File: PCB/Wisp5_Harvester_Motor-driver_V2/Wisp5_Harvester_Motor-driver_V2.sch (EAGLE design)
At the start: 27 parts, among them M1 PINHEAD_PINHD-1X2-1.27MM, M2 PINHEAD_PINHD-1X2-1.27MM, U1 BQ25570

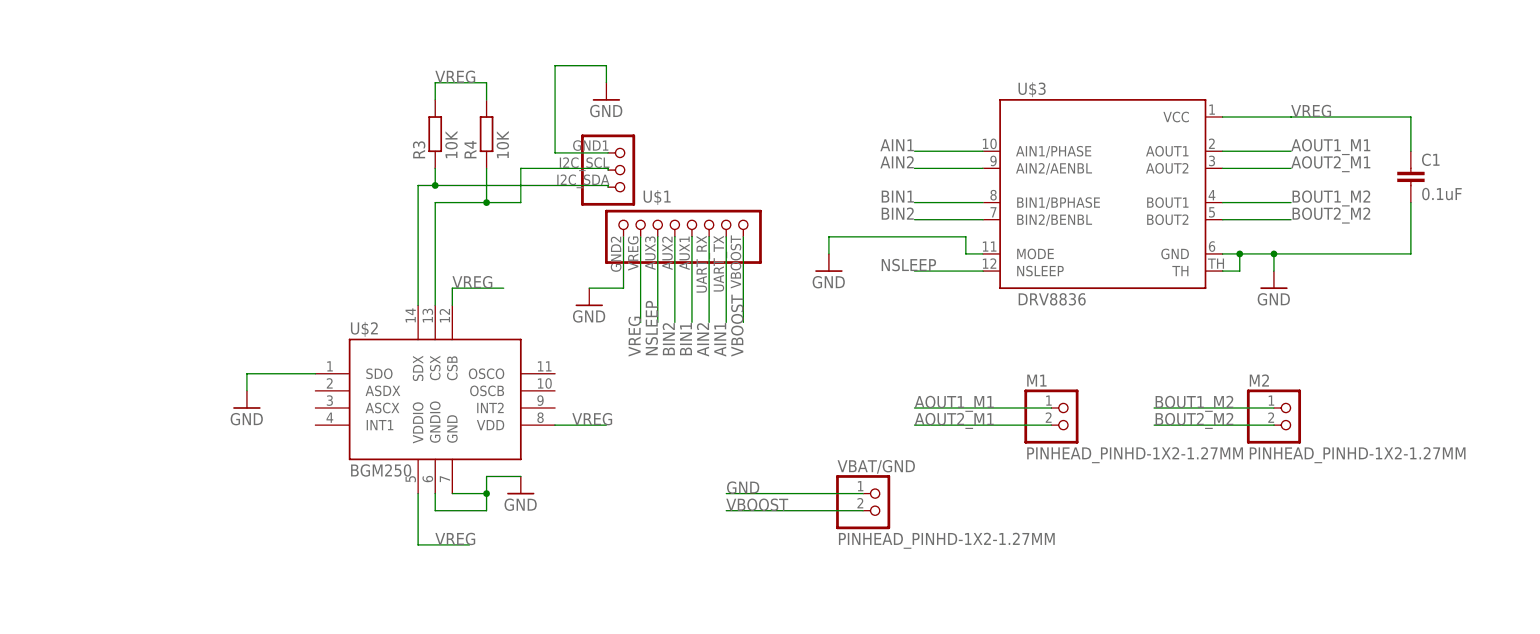
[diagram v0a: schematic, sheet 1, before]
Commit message: Added proximity header and fixed layout
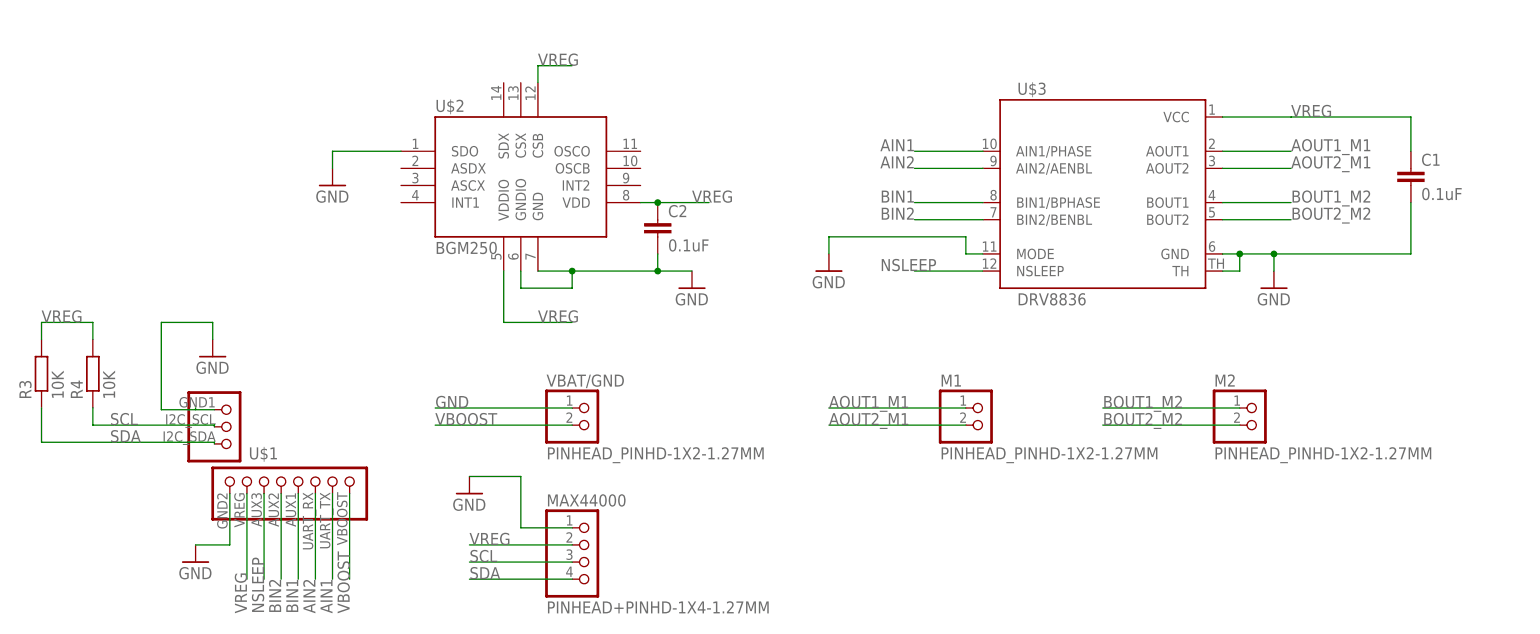
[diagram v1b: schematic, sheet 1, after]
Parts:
- added C2: 0.1uF, rcl:C-EUC0805
- added MAX44000: PINHEAD+PINHD-1X4-1.27MM, Wisp5_Harvester_Motor-driver_V2:PINHEAD+PINHD-1X4-1.27MM
- L1: value (none) -> 22uH
- L2: value (none) -> 10uH
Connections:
- net GND: now also C2.2, MAX44000.1
- net SCL: now also MAX44000.3; no longer U$2.CSX
- net SDA: now also MAX44000.4; no longer U$2.SDX
- net VREG: now also C2.1, MAX44000.2
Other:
- moved on the sheet: M1, M2, R3, R4, U$1, U$2, VBAT/GND

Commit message: Update schematic
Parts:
- U$3: device robot_pcb2:DRV8836 -> Wisp5_Harvester_Motor-driver_V2:DRV8836
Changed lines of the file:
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@@
 </classes>
 <parts>
-<part name="U$3" library="robot_pcb2" deviceset="DRV8836" device=""/>
+<part name="U$3" library="Wisp5_Harvester_Motor-driver_V2" deviceset="DRV8836" device=""/>
 <part name="U1" library="texas" deviceset="BQ25570" device=""/>
 <part name="GND1" library="supply1" deviceset="GND" device=""/>

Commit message: Updated packages
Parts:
- U$3: device Wisp5_Harvester_Motor-driver_V2:DRV8836 -> robot_pcb2:DRV8836
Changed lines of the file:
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@@
 </classes>
 <parts>
-<part name="U$3" library="Wisp5_Harvester_Motor-driver_V2" deviceset="DRV8836" device=""/>
+<part name="U$3" library="robot_pcb2" deviceset="DRV8836" device=""/>
 <part name="U1" library="texas" deviceset="BQ25570" device=""/>
 <part name="GND1" library="supply1" deviceset="GND" device=""/>

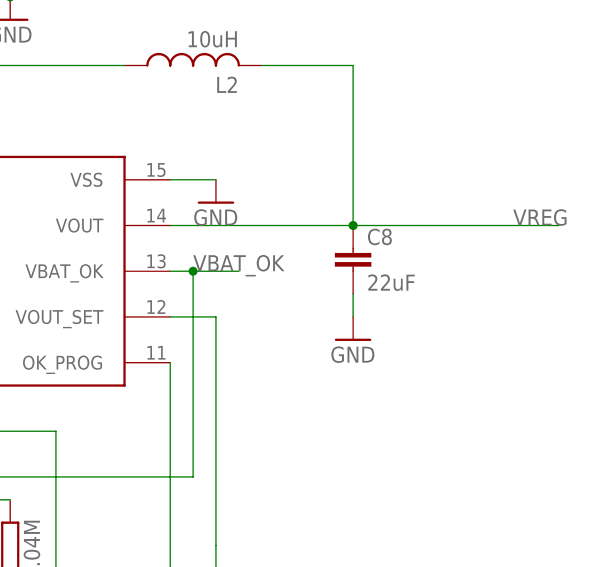
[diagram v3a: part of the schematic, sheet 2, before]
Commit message: Change bulk capacitor from 805 to 1210
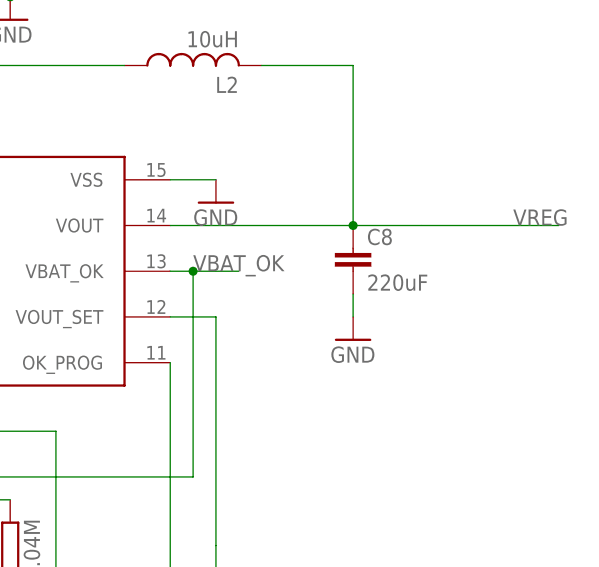
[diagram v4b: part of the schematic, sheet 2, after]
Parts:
- C8: value 22uF -> 220uF; device rcl:C-EUC0805 -> Wisp5_Harvester_Motor-driver_V2:C-EUC1210
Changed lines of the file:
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@@
 <part name="L1" library="robot_pcb2" deviceset="COILCRAFT-LPS4018" device="" value="22uH"/>
 <part name="L2" library="robot_pcb2" deviceset="COILCRAFT-LPS4018" device="" value="10uH"/>
-<part name="C8" library="rcl" deviceset="C-EU" device="C0805" value="22uF"/>
+<part name="C8" library="Wisp5_Harvester_Motor-driver_V2" deviceset="C-EU" device="C1210" value="220uF"/>
 <part name="R6" library="resistor" deviceset="R-EU_" device="R0805" value="6.04M"/>
 <part name="R7" library="resistor" deviceset="R-EU_" device="R0805" value="3.01M"/>

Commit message: Removed some small separate packages
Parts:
- C9: device ipr:BZ054B223ZSBBQ -> Wisp5_Harvester_Motor-driver_V2:BZ054B223ZSBBQ
- U$2: device robot_pcb2:BGM250 -> Wisp5_Harvester_Motor-driver_V2:BGM250
- U1: device texas:BQ25570 -> Wisp5_Harvester_Motor-driver_V2:BQ25570
- VIN/GND: device transceiver:PINHEAD_PINHD-1X2-1.27MM -> Wisp5_Harvester_Motor-driver_V2:PINHEAD_PINHD-1X2-1.27MM
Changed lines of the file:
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@@
 <parts>
 <part name="U$3" library="robot_pcb2" deviceset="DRV8836" device=""/>
-<part name="U1" library="texas" deviceset="BQ25570" device=""/>
+<part name="U1" library="Wisp5_Harvester_Motor-driver_V2" deviceset="BQ25570" device=""/>
 <part name="GND1" library="supply1" deviceset="GND" device=""/>
 <part name="GND5" library="supply1" deviceset="GND" device=""/>
@@
 <part name="GND21" library="supply1" deviceset="GND" device=""/>
 <part name="C4" library="rcl" deviceset="C-EU" device="C0805" value="0.1uF"/>
-<part name="C9" library="ipr" deviceset="BZ054B223ZSBBQ" device=""/>
+<part name="C9" library="Wisp5_Harvester_Motor-driver_V2" deviceset="BZ054B223ZSBBQ" device=""/>
 <part name="R3" library="resistor" deviceset="R-EU_" device="R0805" value="10K"/>
 <part name="R4" library="resistor" deviceset="R-EU_" device="R0805" value="10K"/>
 <part name="GND13" library="supply1" deviceset="GND" device=""/>
 <part name="C1" library="rcl" deviceset="C-EU" device="C0805" value="0.1uF"/>
-<part name="VIN/GND" library="transceiver" deviceset="PINHEAD_PINHD-1X2-1.27MM" device=""/>
+<part name="VIN/GND" library="Wisp5_Harvester_Motor-driver_V2" deviceset="PINHEAD_PINHD-1X2-1.27MM" device=""/>
 <part name="U$1" library="robot_pcb2" deviceset="WISP_HEADER" device=""/>
-<part name="U$2" library="robot_pcb2" deviceset="BGM250" device=""/>
+<part name="U$2" library="Wisp5_Harvester_Motor-driver_V2" deviceset="BGM250" device=""/>
 <part name="GND2" library="supply1" deviceset="GND" device=""/>
 <part name="GND3" library="supply1" deviceset="GND" device=""/>

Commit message: Changed output pins so they work with wisp timer directly and also changed M2 (right)  ground and power order
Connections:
- net AIN1: now also U$1.AUX3; no longer U$1.UART_TX
- net AIN2: now also U$1.AUX1; no longer U$1.UART_RX
- net BIN1: now also U$1.AUX2; no longer U$1.AUX1
- net BIN2: now also U$1.UART_TX; no longer U$1.AUX2
- net BOUT1_M2: now also M2.2; no longer M2.1
- net BOUT2_M2: now also M2.1; no longer M2.2
- net NSLEEP: now also U$1.UART_RX; no longer U$1.AUX3
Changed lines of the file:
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@@
 </segment>
 <segment>
-<pinref part="M2" gate="G$1" pin="1"/>
-<wire x1="180.34" y1="35.56" x2="160.02" y2="35.56" width="0.1524" layer="91"/>
-<label x="160.02" y="35.56" size="1.778" layer="95"/>
+<pinref part="M2" gate="G$1" pin="2"/>
+<wire x1="180.34" y1="33.02" x2="160.02" y2="33.02" width="0.1524" layer="91"/>
+<label x="160.02" y="33.02" size="1.778" layer="95"/>
 </segment>
 </net>
@@
 </segment>
 <segment>
-<pinref part="M2" gate="G$1" pin="2"/>
-<wire x1="180.34" y1="33.02" x2="160.02" y2="33.02" width="0.1524" layer="91"/>
-<label x="160.02" y="33.02" size="1.778" layer="95"/>
+<pinref part="M2" gate="G$1" pin="1"/>
+<wire x1="180.34" y1="35.56" x2="160.02" y2="35.56" width="0.1524" layer="91"/>
+<label x="160.02" y="35.56" size="1.778" layer="95"/>
 </segment>
 </net>
@@
 </segment>
 <segment>
-<pinref part="U$1" gate="G$1" pin="AUX3"/>
-<wire x1="35.56" y1="22.86" x2="35.56" y2="10.16" width="0.1524" layer="91"/>
-<label x="35.56" y="5.08" size="1.778" layer="95" rot="R90"/>
+<pinref part="U$1" gate="G$1" pin="UART_RX"/>
+<wire x1="43.18" y1="22.86" x2="43.18" y2="10.16" width="0.1524" layer="91"/>
+<label x="43.18" y="5.08" size="1.778" layer="95" rot="R90"/>
 </segment>
 </net>
@@
 </segment>
 <segment>
-<pinref part="U$1" gate="G$1" pin="AUX2"/>
-<wire x1="38.1" y1="22.86" x2="38.1" y2="10.16" width="0.1524" layer="91"/>
-<label x="38.1" y="5.08" size="1.778" layer="95" rot="R90"/>
+<pinref part="U$1" gate="G$1" pin="UART_TX"/>
+<wire x1="45.72" y1="22.86" x2="45.72" y2="10.16" width="0.1524" layer="91"/>
+<label x="45.72" y="5.08" size="1.778" layer="95" rot="R90"/>
 </segment>
 </net>
@@
 </segment>
 <segment>
-<pinref part="U$1" gate="G$1" pin="AUX1"/>
-<wire x1="40.64" y1="22.86" x2="40.64" y2="10.16" width="0.1524" layer="91"/>
-<label x="40.64" y="5.08" size="1.778" layer="95" rot="R90"/>
+<pinref part="U$1" gate="G$1" pin="AUX2"/>
+<wire x1="38.1" y1="22.86" x2="38.1" y2="10.16" width="0.1524" layer="91"/>
+<label x="38.1" y="5.08" size="1.778" layer="95" rot="R90"/>
 </segment>
 </net>
@@
 </segment>
 <segment>
-<pinref part="U$1" gate="G$1" pin="UART_RX"/>
-<wire x1="43.18" y1="22.86" x2="43.18" y2="10.16" width="0.1524" layer="91"/>
-<label x="43.18" y="5.08" size="1.778" layer="95" rot="R90"/>
+<pinref part="U$1" gate="G$1" pin="AUX1"/>
+<wire x1="40.64" y1="22.86" x2="40.64" y2="10.16" width="0.1524" layer="91"/>
+<label x="40.64" y="5.08" size="1.778" layer="95" rot="R90"/>
 </segment>
 </net>
@@
 </segment>
 <segment>
-<pinref part="U$1" gate="G$1" pin="UART_TX"/>
-<wire x1="45.72" y1="22.86" x2="45.72" y2="10.16" width="0.1524" layer="91"/>
-<label x="45.72" y="5.08" size="1.778" layer="95" rot="R90"/>
+<pinref part="U$1" gate="G$1" pin="AUX3"/>
+<wire x1="35.56" y1="22.86" x2="35.56" y2="10.16" width="0.1524" layer="91"/>
+<label x="35.56" y="5.08" size="1.778" layer="95" rot="R90"/>
 </segment>
 </net>
